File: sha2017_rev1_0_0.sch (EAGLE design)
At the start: 201 parts, among them IC1 CP210X_USB_UART, IC2 AP7215, IC3 ESP32WROOM32, IC4 TP4056, M1 MOTOR10MM, Q3 MMBT2222A, Q4 MMBT2222A, Q5 SI1304 BDL, T1 MOSFET-PCHANNEL, T2 MOSFET-PCHANNEL, T3 MOSFET-PCHANNEL, T4 AO3400, T5 AO3400, T6 AO3400, U1 MPR121QR2, X2 2908-05WB-MG, X4 JST-PH3

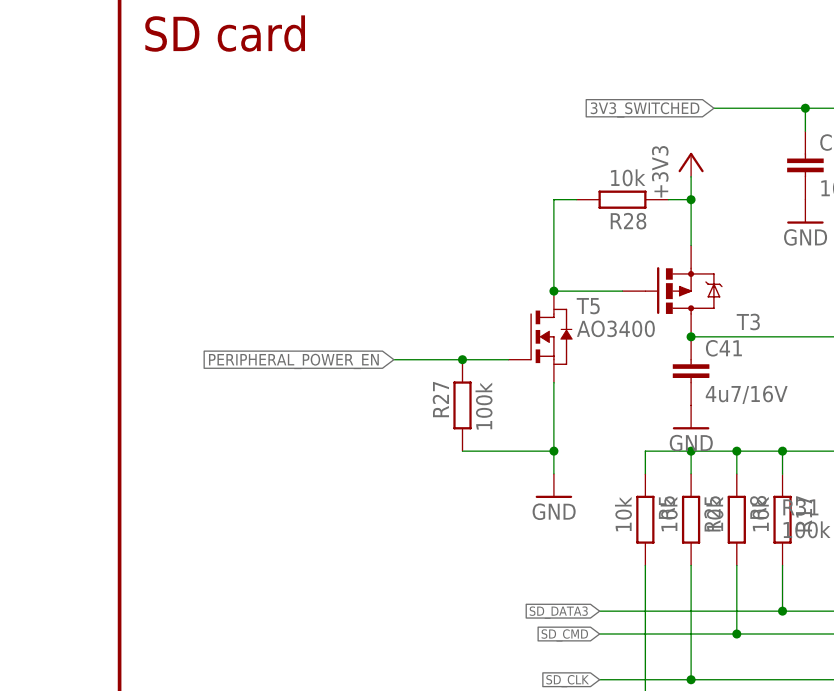
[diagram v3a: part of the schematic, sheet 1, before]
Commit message: Removed unnecessary MOSFETs
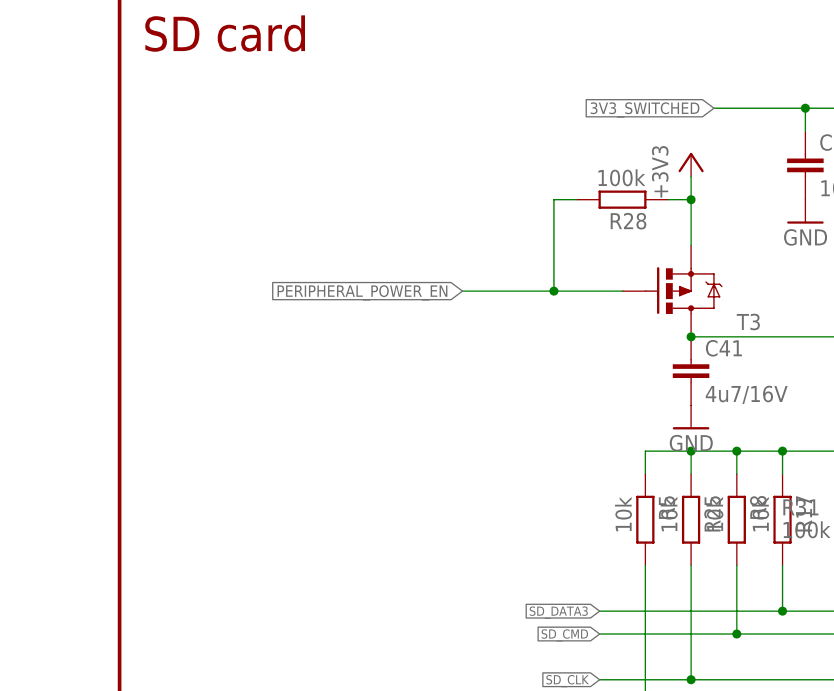
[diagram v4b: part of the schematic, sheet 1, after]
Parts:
- removed R10: 10k, 00ralf:R0603-DASHES
- removed R27: 100k, 00ralf:R0603-DASHES
- removed T5, T6: AO3400, zetex:NMOSSOT23
- R28, R9: value 10k -> 100k
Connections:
- removed net N$17: R28.1, T3.G, T5.D
- removed net N$53: R9.1, T2.G, T6.D
- net GND: no longer R10.2, R27.1, T5.S, T6.S
- net PERIPHERAL_POWER_EN: now also R28.1, R9.1, T2.G, T3.G; no longer R10.1, R27.2, T5.G, T6.G
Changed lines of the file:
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@@
 <setting verticaltext="up"/>
 </settings>
-<grid distance="0.1" unitdist="inch" unit="inch" style="lines" multiple="1" display="no" altdistance="0.01" altunitdist="inch" altunit="inch"/>
+<grid distance="0.05" unitdist="inch" unit="inch" style="lines" multiple="1" display="no" altdistance="0.01" altunitdist="inch" altunit="inch"/>
 <layers>
 <layer number="1" name="Top" color="4" fill="1" visible="no" active="no"/>
@@
 <part name="GND30" library="supply1" deviceset="GND" device=""/>
 <part name="GND38" library="supply1" deviceset="GND" device=""/>
-<part name="R10" library="00ralf" deviceset="R0603-DASHES" device="" value="10k">
+<part name="R9" library="00ralf" deviceset="R0603-DASHES" device="" value="100k">
 <attribute name="PARTNO" value="ERJ-3GEYJ103V"/>
 </part>
-<part name="R9" library="00ralf" deviceset="R0603-DASHES" device="" value="10k">
-<attribute name="PARTNO" value="ERJ-3GEYJ103V"/>
-</part>
-<part name="GND39" library="supply1" deviceset="GND" device=""/>
 <part name="C6" library="sha2017_rev0_1_0_dev" deviceset="C0603-DASHES" device="" value="100n">
 <attribute name="PARTNO" value="GRM188R71H104KA93D"/>
@@
 <attribute name="PARTNO" value="NAP"/>
 </part>
-<part name="R27" library="00ralf" deviceset="R0603-DASHES" device="" value="100k">
+<part name="R28" library="00ralf" deviceset="R0603-DASHES" device="" value="100k">
 <attribute name="PARTNO" value="ERJ-3GEYJ103V"/>
 </part>
-<part name="R28" library="00ralf" deviceset="R0603-DASHES" device="" value="10k">
-<attribute name="PARTNO" value="ERJ-3GEYJ103V"/>
-</part>
-<part name="GND56" library="supply1" deviceset="GND" device=""/>
 <part name="GND57" library="supply1" deviceset="GND" device=""/>
 <part name="+3V6" library="supply1" deviceset="+3V3" device=""/>
@@
 <part name="GND55" library="supply1" deviceset="GND" device=""/>
 <part name="T4" library="zetex" deviceset="NMOSSOT23" device="" value="AO3400"/>
-<part name="T5" library="zetex" deviceset="NMOSSOT23" device="" value="AO3400"/>
-<part name="T6" library="zetex" deviceset="NMOSSOT23" device="" value="AO3400"/>
 </parts>
 <sheets>
@@
 <attribute name="PARTNO" x="38.1" y="10.16" size="5.08" layer="96" display="off"/>
 </instance>
-<instance part="R27" gate="G$1" x="302.26" y="109.22" smashed="yes" rot="R90">
-<attribute name="NAME" x="300.7614" y="112.014" size="1.778" layer="95" rot="MR270"/>
-<attribute name="VALUE" x="305.562" y="111.76" size="1.778" layer="96" rot="MR270"/>
-<attribute name="PARTNO" x="302.26" y="109.22" size="5.08" layer="96" rot="MR90" display="off"/>
-</instance>
 <instance part="R28" gate="G$1" x="320.04" y="132.08" smashed="yes" rot="MR180">
 <attribute name="NAME" x="322.834" y="130.5814" size="1.778" layer="95" rot="R180"/>
@@
 <attribute name="PARTNO" x="320.04" y="132.08" size="5.08" layer="96" display="off"/>
 </instance>
-<instance part="GND56" gate="1" x="312.42" y="99.06" rot="MR0"/>
 <instance part="GND57" gate="1" x="327.66" y="106.68" rot="MR0"/>
 <instance part="+3V6" gate="G$1" x="327.66" y="137.16"/>
@@
 <instance part="P+7" gate="VCC" x="218.44" y="143.51"/>
 <instance part="T4" gate="A" x="218.44" y="104.14"/>
-<instance part="T5" gate="A" x="312.42" y="116.84"/>
 </instances>
 <busses>
@@
 </segment>
 <segment>
-<pinref part="GND56" gate="1" pin="GND"/>
-<wire x1="312.42" y1="101.6" x2="312.42" y2="104.14" width="0.1524" layer="91"/>
-<pinref part="T5" gate="A" pin="S"/>
-<pinref part="R27" gate="G$1" pin="1"/>
-<wire x1="312.42" y1="104.14" x2="312.42" y2="111.76" width="0.1524" layer="91"/>
-<wire x1="302.26" y1="104.14" x2="312.42" y2="104.14" width="0.1524" layer="91"/>
-<junction x="312.42" y="104.14"/>
-</segment>
-<segment>
 <pinref part="S2" gate="G$1" pin="1"/>
 <wire x1="91.44" y1="185.42" x2="88.9" y2="185.42" width="0.1524" layer="91"/>
@@
 </segment>
 </net>
-<net name="N$17" class="0">
-<segment>
-<pinref part="R28" gate="G$1" pin="1"/>
-<wire x1="314.96" y1="132.08" x2="312.42" y2="132.08" width="0.1524" layer="91"/>
-<wire x1="312.42" y1="132.08" x2="312.42" y2="121.92" width="0.1524" layer="91"/>
-<wire x1="312.42" y1="121.92" x2="320.04" y2="121.92" width="0.1524" layer="91"/>
-<pinref part="T3" gate="G$1" pin="G"/>
-<pinref part="T5" gate="A" pin="D"/>
-<junction x="312.42" y="121.92"/>
-</segment>
-</net>
 <net name="3V3_SWITCHED" class="0">
 <segment>
@@
 <net name="PERIPHERAL_POWER_EN" class="0">
 <segment>
-<label x="294.64" y="114.3" size="1.27" layer="95" rot="R180" xref="yes"/>
-<wire x1="302.26" y1="114.3" x2="294.64" y2="114.3" width="0.1524" layer="91"/>
-<pinref part="R27" gate="G$1" pin="2"/>
-<wire x1="307.34" y1="114.3" x2="302.26" y2="114.3" width="0.1524" layer="91"/>
-<junction x="302.26" y="114.3"/>
-<pinref part="T5" gate="A" pin="G"/>
+<label x="302.26" y="121.92" size="1.27" layer="95" rot="R180" xref="yes"/>
+<wire x1="312.42" y1="121.92" x2="302.26" y2="121.92" width="0.1524" layer="91"/>
+<pinref part="R28" gate="G$1" pin="1"/>
+<wire x1="314.96" y1="132.08" x2="312.42" y2="132.08" width="0.1524" layer="91"/>
+<wire x1="312.42" y1="132.08" x2="312.42" y2="121.92" width="0.1524" layer="91"/>
+<wire x1="312.42" y1="121.92" x2="320.04" y2="121.92" width="0.1524" layer="91"/>
+<pinref part="T3" gate="G$1" pin="G"/>
+<junction x="312.42" y="121.92"/>
 </segment>
 </net>
@@
 <instance part="GND30" gate="1" x="227.33" y="209.55"/>
 <instance part="GND38" gate="1" x="300.99" y="209.55"/>
-<instance part="R10" gate="G$1" x="50.8" y="200.66" smashed="yes" rot="MR270">
-<attribute name="NAME" x="49.3014" y="197.866" size="1.778" layer="95" rot="R90"/>
-<attribute name="VALUE" x="54.102" y="198.12" size="1.778" layer="96" rot="R90"/>
-<attribute name="PARTNO" x="50.8" y="200.66" size="5.08" layer="96" rot="R270" display="off"/>
-</instance>
 <instance part="R9" gate="G$1" x="66.04" y="220.98" smashed="yes" rot="MR180">
 <attribute name="NAME" x="68.834" y="219.4814" size="1.778" layer="95" rot="R180"/>
@@
 <attribute name="PARTNO" x="66.04" y="220.98" size="5.08" layer="96" display="off"/>
 </instance>
-<instance part="GND39" gate="1" x="58.42" y="190.5" rot="MR0"/>
 <instance part="C6" gate="G$1" x="132.08" y="227.33" rot="R90">
 <attribute name="PARTNO" x="132.08" y="227.33" size="5.08" layer="96" display="off"/>
@@
 </instance>
 <instance part="GND55" gate="1" x="264.16" y="68.58" rot="MR0"/>
-<instance part="T6" gate="A" x="58.42" y="208.28"/>
 </instances>
 <busses>
@@
 </segment>
 <segment>
-<pinref part="GND39" gate="1" pin="GND"/>
-<wire x1="58.42" y1="193.04" x2="58.42" y2="195.58" width="0.1524" layer="91"/>
-<pinref part="T6" gate="A" pin="S"/>
-<pinref part="R10" gate="G$1" pin="2"/>
-<wire x1="58.42" y1="195.58" x2="58.42" y2="203.2" width="0.1524" layer="91"/>
-<wire x1="50.8" y1="195.58" x2="58.42" y2="195.58" width="0.1524" layer="91"/>
-<junction x="58.42" y="195.58"/>
-</segment>
-<segment>
 <pinref part="C6" gate="G$1" pin="1"/>
 <pinref part="GND40" gate="1" pin="GND"/>
@@
 </segment>
 </net>
-<net name="N$53" class="0">
-<segment>
-<pinref part="R9" gate="G$1" pin="1"/>
-<wire x1="60.96" y1="220.98" x2="58.42" y2="220.98" width="0.1524" layer="91"/>
-<wire x1="58.42" y1="220.98" x2="58.42" y2="213.36" width="0.1524" layer="91"/>
-<wire x1="58.42" y1="213.36" x2="68.58" y2="213.36" width="0.1524" layer="91"/>
-<pinref part="T2" gate="G$1" pin="G"/>
-<pinref part="T6" gate="A" pin="D"/>
-<junction x="58.42" y="213.36"/>
-</segment>
-</net>
 <net name="WS2812_DATA" class="0">
 <segment>
@@
 <net name="PERIPHERAL_POWER_EN" class="0">
 <segment>
-<pinref part="R10" gate="G$1" pin="1"/>
-<wire x1="50.8" y1="205.74" x2="40.64" y2="205.74" width="0.1524" layer="91"/>
-<label x="40.64" y="205.74" size="1.27" layer="95" rot="R180" xref="yes"/>
-<pinref part="T6" gate="A" pin="G"/>
-<wire x1="50.8" y1="205.74" x2="53.34" y2="205.74" width="0.1524" layer="91"/>
-<junction x="50.8" y="205.74"/>
+<wire x1="58.42" y1="213.36" x2="41.91" y2="213.36" width="0.1524" layer="91"/>
+<label x="41.91" y="213.36" size="1.27" layer="95" rot="R180" xref="yes"/>
+<pinref part="R9" gate="G$1" pin="1"/>
+<wire x1="60.96" y1="220.98" x2="58.42" y2="220.98" width="0.1524" layer="91"/>
+<wire x1="58.42" y1="220.98" x2="58.42" y2="213.36" width="0.1524" layer="91"/>
+<wire x1="58.42" y1="213.36" x2="68.58" y2="213.36" width="0.1524" layer="91"/>
+<pinref part="T2" gate="G$1" pin="G"/>
+<junction x="58.42" y="213.36"/>
 </segment>
 <segment>

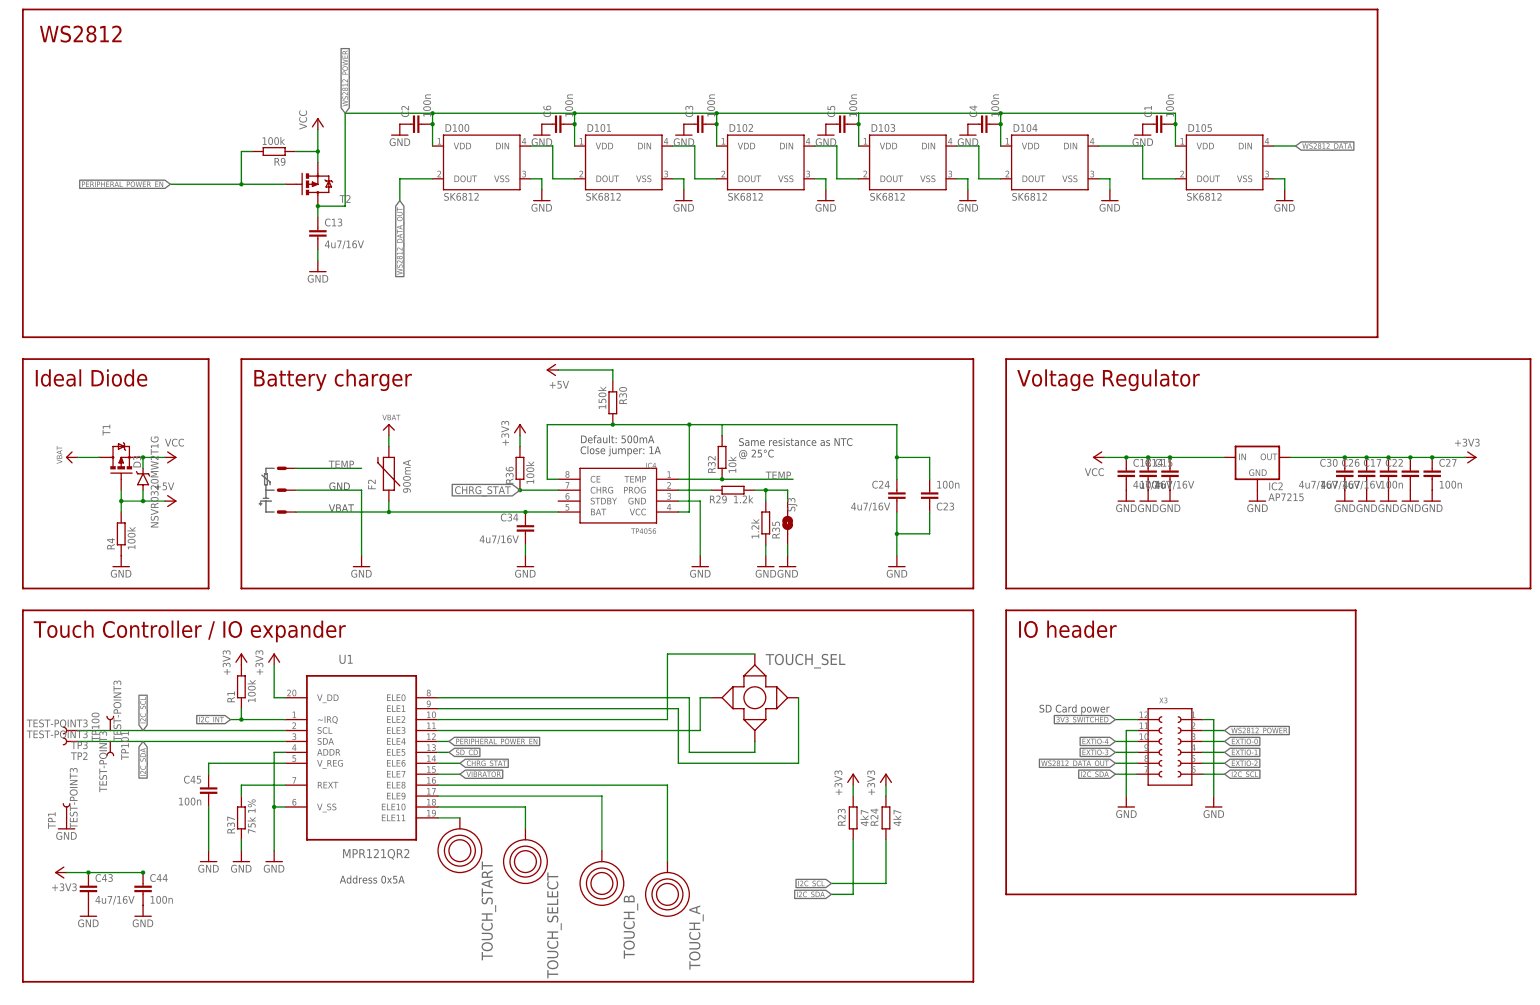
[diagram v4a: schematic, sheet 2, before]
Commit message: Finalized LED and SD card power switches, rerouted
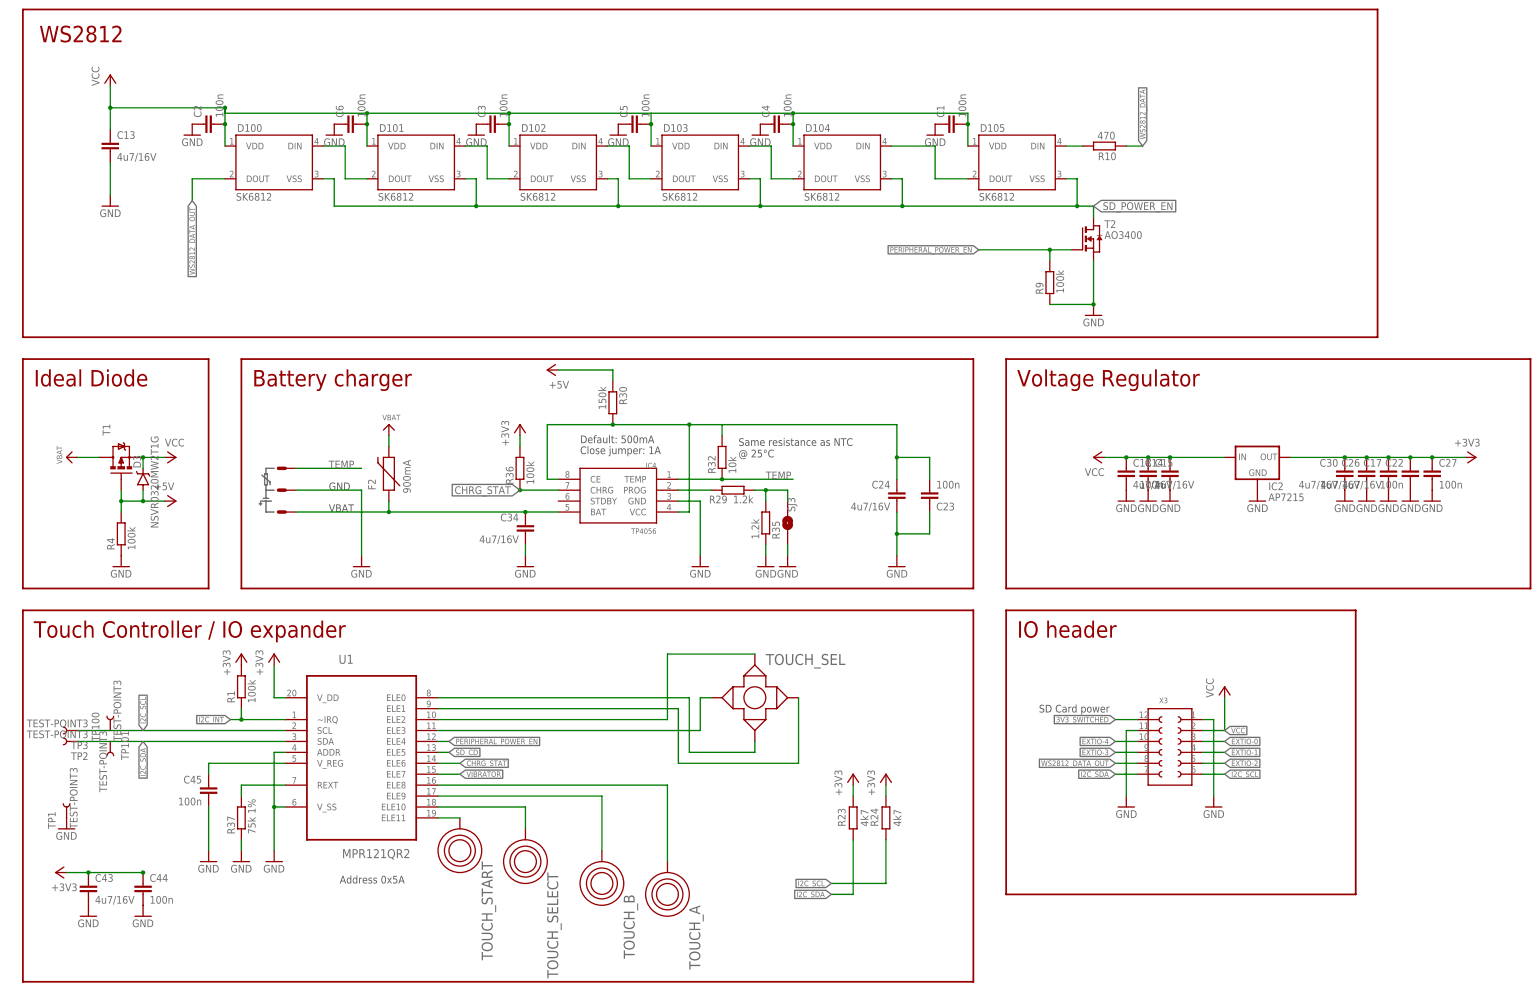
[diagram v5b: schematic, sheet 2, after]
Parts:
- added R10: 470, 00ralf:R0603-DASHES
- T2: value MOSFET-PCHANNEL -> AO3400; device SparkFun-DiscreteSemi:MOSFET-PCHANNEL -> zetex:NMOSSOT23
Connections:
- new net N$15: D105.DIN, R10.1
- new net SD_POWER_EN: D100.VSS, D101.VSS, D102.VSS, D103.VSS, D104.VSS, D105.VSS, R28.1, T2.D, T3.G
- net GND: now also R9.2, T2.S; no longer D100.VSS, D101.VSS, D102.VSS, D103.VSS, D104.VSS, D105.VSS
- net PERIPHERAL_POWER_EN: no longer R28.1, T3.G
- net VCC: now also C1.2, C13.1, C2.2, C3.2, C4.2, C5.2, C6.2, D100.VDD, D101.VDD, D102.VDD, D103.VDD, D104.VDD, D105.VDD, X3.11; no longer R9.2, T2.S
- net WS2812_DATA: now also R10.2; no longer D105.DIN
- net WS2812_POWER: no longer C1.2, C13.1, C2.2, C3.2, C4.2, C5.2, C6.2, D100.VDD, D101.VDD, D102.VDD, D103.VDD, D104.VDD, D105.VDD, T2.D, X3.11
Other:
- moved on the sheet: C1, C13, C2, C3, C4, C5, C6, D100, D101, D102, D103, D104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

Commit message: Reroute touch controller
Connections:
- removed net WS2812_POWER: TP117.1
- net VCC: now also TP117.1
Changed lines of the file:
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@@
-</segment>
-</net>
-<net name="WS2812_POWER" class="0">
-<segment>
-<pinref part="TP117" gate="G$1" pin="1"/>
-<wire x1="43.18" y1="137.16" x2="38.1" y2="137.16" width="0.1524" layer="91"/>
-<label x="38.1" y="137.16" size="1.27" layer="95" rot="R180" xref="yes"/>
 </segment>
 </net>
@@
 <label x="68.58" y="152.4" size="1.27" layer="95" rot="R180" xref="yes"/>
 </segment>
+<segment>
+<pinref part="TP117" gate="G$1" pin="1"/>
+<wire x1="43.18" y1="137.16" x2="38.1" y2="137.16" width="0.1524" layer="91"/>
+<label x="38.1" y="137.16" size="1.27" layer="95" rot="R180" xref="yes"/>
+</segment>
 </net>
